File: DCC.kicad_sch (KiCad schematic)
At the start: 9 parts, among them J701 DB15_Female, J702 DB9_Female, J703 DB25_Female_MountingHoles, J704 DB37_Female_MountingHoles, U701 6N137

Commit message: made additions to the project
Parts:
- removed J701: DB15_Female, Connector_Dsub:DSUB-15_Female_Horizontal_P2.77x2.54mm_EdgePinOffset9.40mm, symbol Connector:DB15_Female
- removed J702: DB9_Female, Connector_Dsub:DSUB-9_Female_Horizontal_P2.77x2.54mm_EdgePinOffset9.40mm, symbol Connector:DB9_Female
- removed J703: DB25_Female_MountingHoles, Connector_Dsub:DSUB-25_Female_Horizontal_P2.77x2.84mm_EdgePinOffset9.90mm_Housed_MountingHolesOffset11.32mm, symbol Connector:DB25_Female_MountingHoles
- removed J704: DB37_Female_MountingHoles, Connector_Dsub:DSUB-37_Female_Horizontal_P2.77x2.84mm_EdgePinOffset14.56mm_Housed_MountingHolesOffset8.20mm, symbol Connector:DB37_Female_MountingHoles
- R701: value 1k -> 10k; footprint (none) -> Resistor_SMD:R_0805_2012Metric_Pad1.20x1.40mm_HandSolder; JLCPCB Part# (none) -> C17414
- R702: footprint (none) -> Resistor_SMD:R_0805_2012Metric_Pad1.20x1.40mm_HandSolder; JLCPCB Part# (none) -> C17414
- R703: value 10k -> 1k; footprint (none) -> Resistor_SMD:R_0805_2012Metric_Pad1.20x1.40mm_HandSolder; JLCPCB Part# (none) -> C17513
- U701: footprint Package_DIP:DIP-8_W7.62mm -> Package_SO:SOP-8_6.62x9.15mm_P2.54mm; JLCPCB Part# (none) -> C110020
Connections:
- net +5V: now also R701.1; no longer R703.1
- net DCC_A: now also R703.1; no longer R701.1
- net at D701.1 (K), U701.2 (A): now also R703.2; no longer R701.2
- net at U701.7 (EN): now also R701.2; no longer R702.2
- net PIN2 renamed DCC_IN
- net DCC_IN: now also R702.2; no longer R703.2

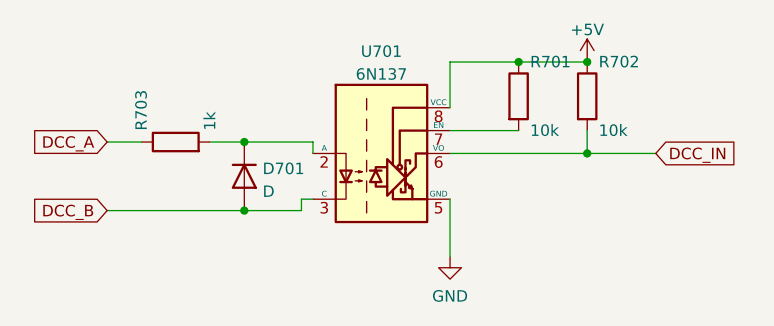
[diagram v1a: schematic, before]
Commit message: added hierarchial labels to some schematics
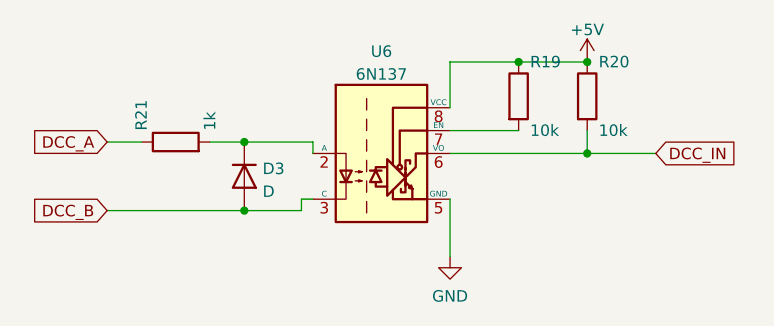
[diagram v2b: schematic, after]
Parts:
- renumbered D701 to D3, R701 to R19, R702 to R20, R703 to R21, U701 to U6

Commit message: moved some schematic scheets to their own folders and routed a board with it. This allow for re-use of PCB parts.
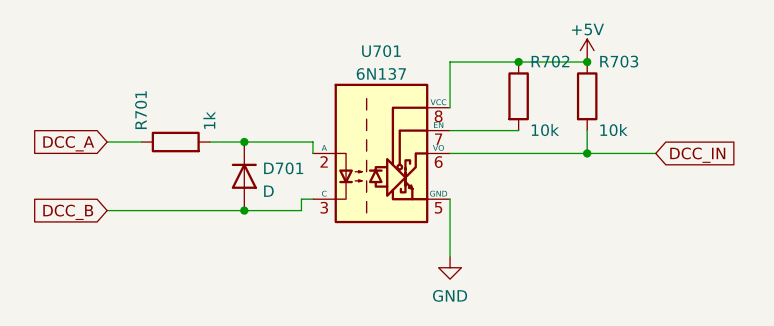
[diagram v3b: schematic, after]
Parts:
- renumbered D3 to D701, R21 to R701, R19 to R702, R20 to R703, U6 to U701
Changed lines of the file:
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@@
   (symbol (lib_id "power:GND") (at 135.89 107.95 0) (unit 1)
     (in_bom yes) (on_board yes) (dnp no) (fields_autoplaced)
-    (property "Reference" "#PWR026" (at 135.89 114.3 0)
+    (property "Reference" "#PWR0112" (at 135.89 114.3 0)
       (effects (font (size 1.27 1.27)) hide)
     )
@@
       (project "general_schematics"
         (path "/e777d9ec-d073-4229-a9e6-2cf85636e407/c3ae8e23-d3b7-46ce-84c2-3bde61a5ce74"
-          (reference "#PWR026") (unit 1)
+          (reference "#PWR0112") (unit 1)
         )
       )
@@
   (symbol (lib_id "power:+5V") (at 151.13 86.36 0) (unit 1)
     (in_bom yes) (on_board yes) (dnp no) (fields_autoplaced)
-    (property "Reference" "#PWR025" (at 151.13 90.17 0)
+    (property "Reference" "#PWR0111" (at 151.13 90.17 0)
       (effects (font (size 1.27 1.27)) hide)
     )
@@
       (project "general_schematics"
         (path "/e777d9ec-d073-4229-a9e6-2cf85636e407/c3ae8e23-d3b7-46ce-84c2-3bde61a5ce74"
-          (reference "#PWR025") (unit 1)
+          (reference "#PWR0111") (unit 1)
         )
       )
@@
   (symbol (lib_id "Device:R") (at 143.51 90.17 0) (unit 1)
     (in_bom yes) (on_board yes) (dnp no)
-    (property "Reference" "R19" (at 144.78 86.36 0)
+    (property "Reference" "R702" (at 144.78 86.36 0)
       (effects (font (size 1.27 1.27)) (justify left))
     )
@@
       (project "general_schematics"
         (path "/e777d9ec-d073-4229-a9e6-2cf85636e407/c3ae8e23-d3b7-46ce-84c2-3bde61a5ce74"
-          (reference "R19") (unit 1)
+          (reference "R702") (unit 1)
         )
       )
@@
   (symbol (lib_id "Device:R") (at 105.41 95.25 90) (unit 1)
     (in_bom yes) (on_board yes) (dnp no)
-    (property "Reference" "R21" (at 101.6 93.98 0)
+    (property "Reference" "R701" (at 101.6 93.98 0)
       (effects (font (size 1.27 1.27)) (justify left))
     )
@@
       (project "general_schematics"
         (path "/e777d9ec-d073-4229-a9e6-2cf85636e407/c3ae8e23-d3b7-46ce-84c2-3bde61a5ce74"
-          (reference "R21") (unit 1)
+          (reference "R701") (unit 1)
         )
       )
@@
   (symbol (lib_id "Device:D") (at 113.03 99.06 270) (unit 1)
     (in_bom yes) (on_board yes) (dnp no) (fields_autoplaced)
-    (property "Reference" "D3" (at 115.062 98.2253 90)
+    (property "Reference" "D701" (at 115.062 98.2253 90)
       (effects (font (size 1.27 1.27)) (justify left))
     )
@@
       (project "general_schematics"
         (path "/e777d9ec-d073-4229-a9e6-2cf85636e407/c3ae8e23-d3b7-46ce-84c2-3bde61a5ce74"
-          (reference "D3") (unit 1)
+          (reference "D701") (unit 1)
         )
       )
@@
   (symbol (lib_id "Device:R") (at 151.13 90.17 0) (unit 1)
     (in_bom yes) (on_board yes) (dnp no)
-    (property "Reference" "R20" (at 152.4 86.36 0)
+    (property "Reference" "R703" (at 152.4 86.36 0)
       (effects (font (size 1.27 1.27)) (justify left))
     )
@@
       (project "general_schematics"
         (path "/e777d9ec-d073-4229-a9e6-2cf85636e407/c3ae8e23-d3b7-46ce-84c2-3bde61a5ce74"
-          (reference "R20") (unit 1)
+          (reference "R703") (unit 1)
         )
       )
@@
   (symbol (lib_id "Isolator:6N137") (at 128.27 96.52 0) (unit 1)
     (in_bom yes) (on_board yes) (dnp no) (fields_autoplaced)
-    (property "Reference" "U6" (at 128.27 85.2002 0)
+    (property "Reference" "U701" (at 128.27 85.2002 0)
       (effects (font (size 1.27 1.27)))
     )
@@
       (project "general_schematics"
         (path "/e777d9ec-d073-4229-a9e6-2cf85636e407/c3ae8e23-d3b7-46ce-84c2-3bde61a5ce74"
-          (reference "U6") (unit 1)
+          (reference "U701") (unit 1)
         )
       )
